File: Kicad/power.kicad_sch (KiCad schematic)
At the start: 8 parts, among them U1 MP1584, U2 LM317_TO-252, U3 AMS1117-3.3

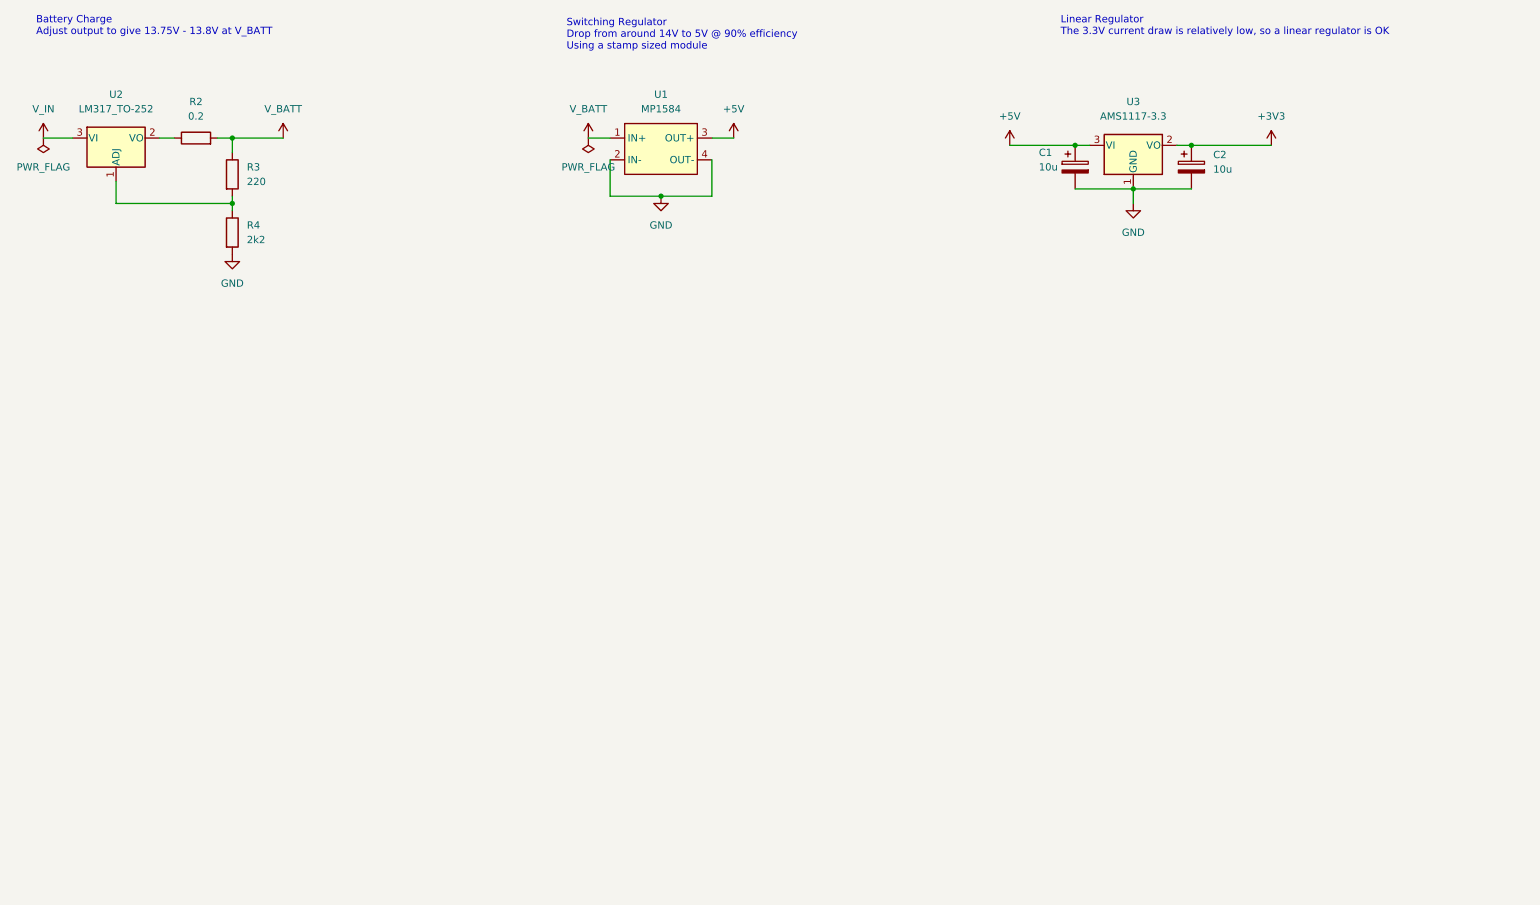
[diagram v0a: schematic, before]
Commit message: Rework of power circuits to improve protection
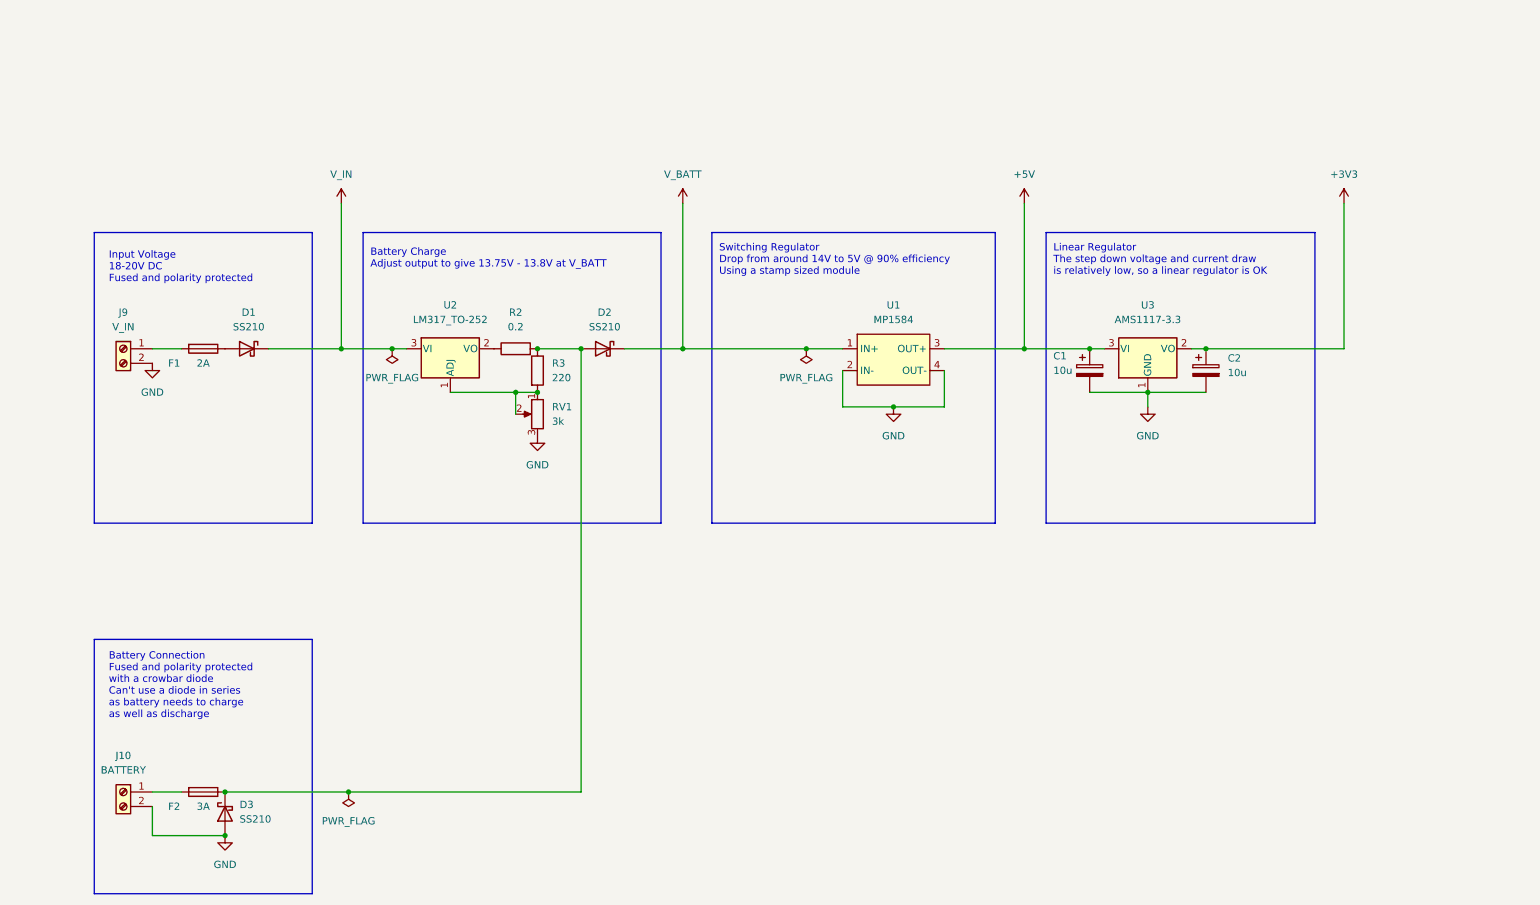
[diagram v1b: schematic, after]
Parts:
- removed R4: 2k2, Resistor_SMD:R_0603_1608Metric, symbol Device:R
- added D1, D2, D3: SS210, Diode_SMD:D_SMA, symbol Device:D_Schottky
- added F1: 2A, Fuse:Fuseholder_Cylinder-5x20mm_Schurter_0031_8201_Horizontal_Open, symbol Device:Fuse
- added F2: 3A, Fuse:Fuseholder_Cylinder-5x20mm_Schurter_0031_8201_Horizontal_Open, symbol Device:Fuse
- added J10: BATTERY, TerminalBlock_Phoenix:TerminalBlock_Phoenix_MPT-0,5-2-2.54_1x02_P2.54mm_Horizontal, symbol Connector:Screw_Terminal_01x02
- added J9: V_IN, TerminalBlock_Phoenix:TerminalBlock_Phoenix_MPT-0,5-2-2.54_1x02_P2.54mm_Horizontal, symbol Connector:Screw_Terminal_01x02
- added RV1: 3k, Potentiometer_THT:Potentiometer_Bourns_3296W_Vertical, symbol Device:R_Potentiometer
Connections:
- net +BATT: now also D2.1 (K); no longer R2.2, R3.1
- net GND: now also D3.2 (A), J10.2 (Pin_2), J9.2 (Pin_2), RV1.3
- net V_IN: now also D1.1 (K)
- net at R3.2, U2.1 (ADJ): now also RV1.1, RV1.2
- new net: D1.2 (A), F1.1
- new net: F1.2, J9.1 (Pin_1)
- new net: D2.2 (A), D3.1 (K), F2.1, R2.2, R3.1
- new net: F2.2, J10.1 (Pin_1)
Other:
- note added: "Battery Connection Fused and polarity protected with a crowbar diode Can't use a diode in series as battery needs to charge as well as discharge"
- note added: "Input Voltage 18-20V DC Fused and polarity protected"
- note added: "Linear Regulator The step down voltage and current draw is relatively low, so a linear regulator is OK"
- note removed: "Linear Regulator The 3.3V current draw is relatively low, so a linear regulator is OK"
- moved on the sheet: C1, C2, R2, R3, U1, U2, U3
